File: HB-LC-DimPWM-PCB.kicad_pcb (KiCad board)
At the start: 2 copper layers, 73 parts, among them J1 SWD, J3 Conn_01x04_Male, Q1 S9013, Q10 BSS84, Q11 2N7002, Q12 BSS84, Q13 2N7002, Q14 VS5810AS, Q15 VS5810AS, Q16 VS5810AS, Q2 BSS84, Q3 2N7002, Q4 VS5810AS, Q5 S9013, Q6 S9013, Q7 S9013, Q8 BSS84, Q9 2N7002, U1 STM32F103C8Tx, U2 AMS1117-3.3, Y1 8MHz

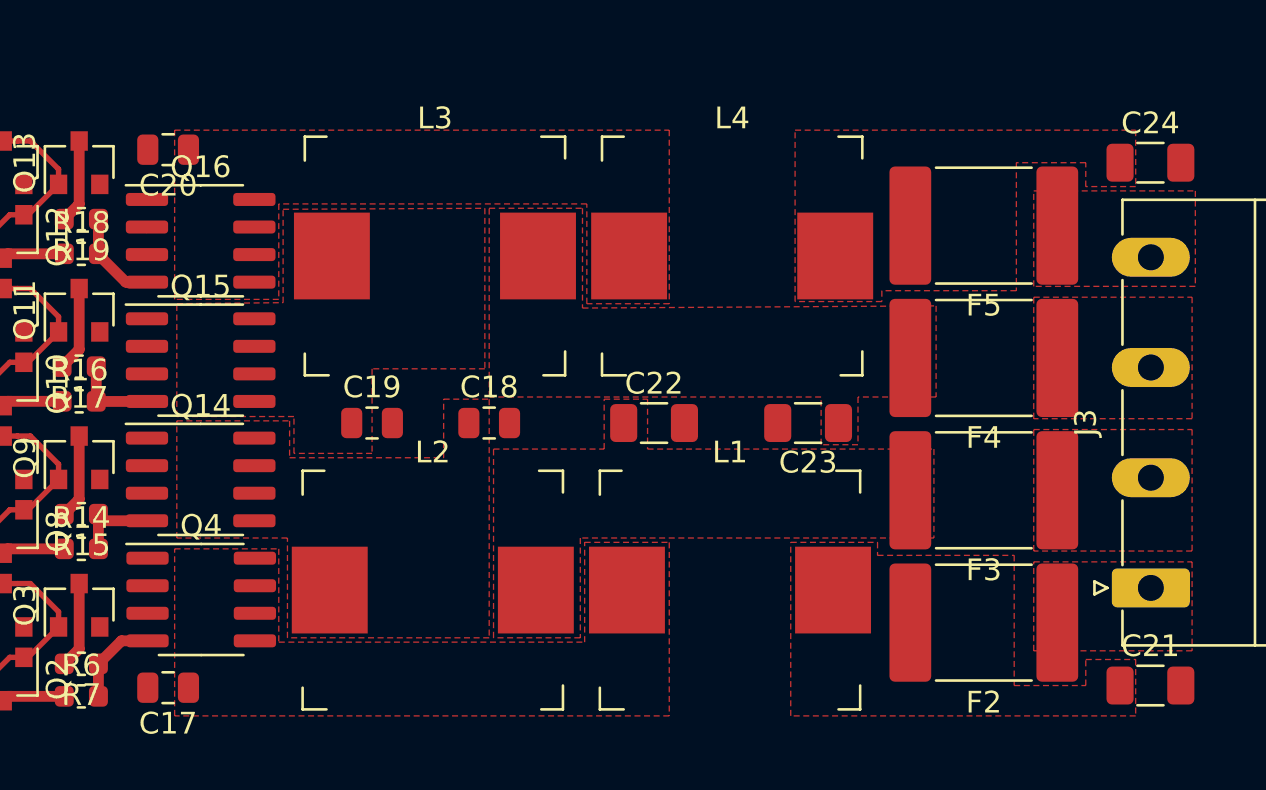
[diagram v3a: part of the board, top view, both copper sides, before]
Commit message: Add more space for GND vias below dimmer FETs
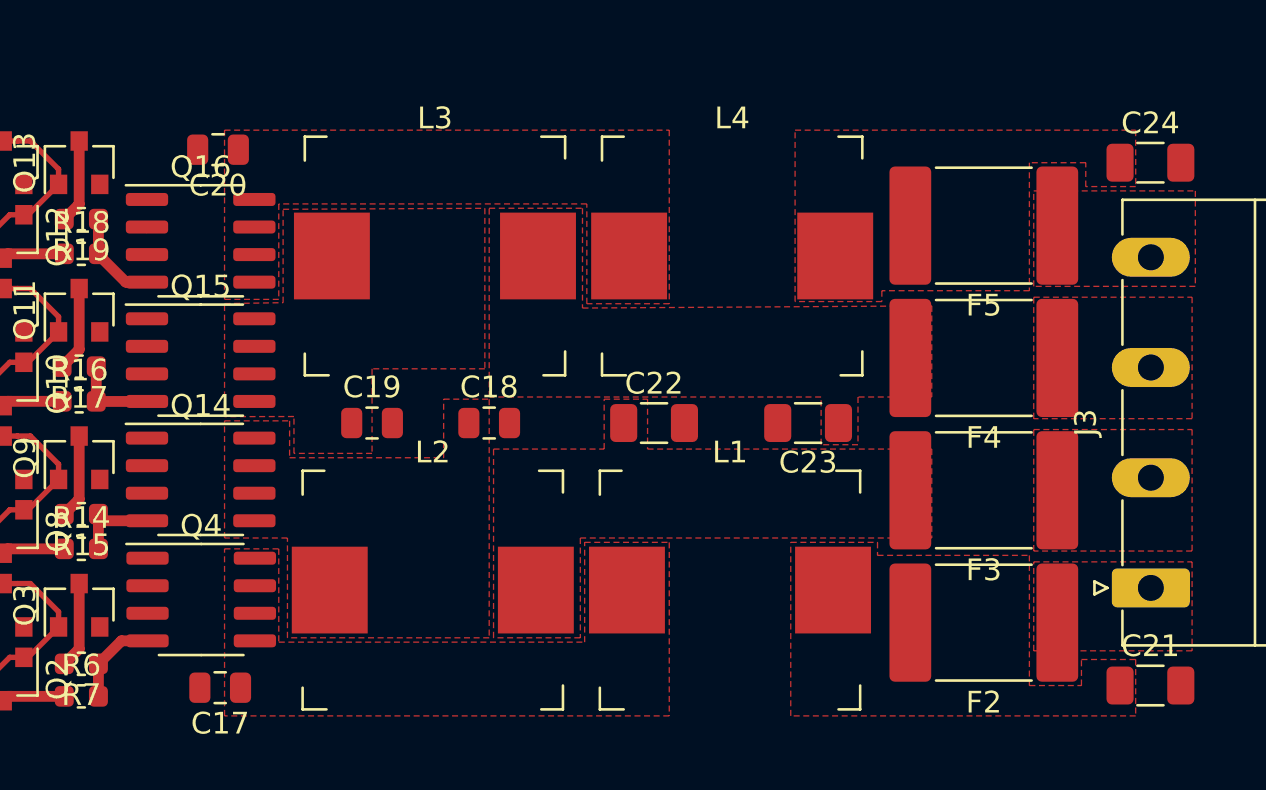
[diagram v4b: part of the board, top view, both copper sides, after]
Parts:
- moved C17 2.40 mm to (122.3, 92.6)
- moved C20 2.30 mm to (122.2, 67.8)
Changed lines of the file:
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@@
   )
   (module Capacitor_SMD:C_0805_2012Metric (layer F.Cu)
-    (at 119.9 67.8 180)
+    (at 122.2 67.8 180)
     (descr "Capacitor SMD 0805 (2012 Metric), square (rectangular) end terminal, IPC_7351 nominal, (Body size source: https://docs.google.com/spreadsheets/d/1BsfQQcO9C6DZCsRaXUlFlo91Tg2WpOkGARC1WS5S8t0/edit?usp=sharing), generated with kicad-footprint-generator")
     (tags capacitor)
@@
   )
   (module Capacitor_SMD:C_0805_2012Metric (layer F.Cu)
-    (at 119.9 92.6 180)
+    (at 122.3 92.6 180)
     (descr "Capacitor SMD 0805 (2012 Metric), square (rectangular) end terminal, IPC_7351 nominal, (Body size source: https://docs.google.com/spreadsheets/d/1BsfQQcO9C6DZCsRaXUlFlo91Tg2WpOkGARC1WS5S8t0/edit?usp=sharing), generated with kicad-footprint-generator")
     (tags capacitor)
@@
       (pts
         (xy 134.5 77.9) (xy 129.3 77.9) (xy 129.3 81.8) (xy 125.7 81.8) (xy 125.7 80.1)
-        (xy 120.3 80.1) (xy 120.3 74.9) (xy 125.2 74.852106) (xy 125.2 70.547894) (xy 134.5 70.501404)
+        (xy 122.5 80.105506) (xy 122.5 74.894494) (xy 125.2 74.852106) (xy 125.2 70.547894) (xy 134.5 70.501404)
       )
     )
@@
       (pts
         (xy 143 74.9) (xy 139.2 74.9) (xy 139.2 70.3) (xy 125 70.3) (xy 125.000533 74.7)
-        (xy 120.199467 74.7) (xy 120.2 66.9) (xy 143 66.9)
+        (xy 122.499734 74.7) (xy 122.500267 66.9) (xy 143 66.9)
       )
     )
@@
       (pts
         (xy 125.5 82) (xy 132.6 82) (xy 132.6 79.3) (xy 134.7 79.3) (xy 134.7 90.3)
-        (xy 125.4 90.3) (xy 125.4 85.7) (xy 120.3 85.700354) (xy 120.3 80.299646) (xy 125.5 80.300354)
+        (xy 125.4 90.3) (xy 125.4 85.7) (xy 122.5 85.700354) (xy 122.5 80.299646) (xy 125.5 80.300354)
       )
     )
@@
     (polygon
       (pts
-        (xy 143 93.9) (xy 120.2 93.9) (xy 120.2 86.2) (xy 125 86.2) (xy 125 90.5)
+        (xy 143 93.9) (xy 122.5 93.9) (xy 122.5 86.2) (xy 125 86.2) (xy 125 90.5)
         (xy 139.1 90.5) (xy 139.1 85.9) (xy 143 85.9)
       )
@@
     (polygon
       (pts
-        (xy 155.2 85.7) (xy 138.9 85.7) (xy 138.9 90.3) (xy 134.9 90.3) (xy 134.9 81.6)
-        (xy 140 81.6) (xy 140 79.3) (xy 142 79.3) (xy 142 81.6) (xy 155.2 81.6)
+        (xy 155.1 85.7) (xy 138.9 85.7) (xy 138.9 90.3) (xy 134.9 90.3) (xy 134.9 81.6)
+        (xy 140 81.6) (xy 140 79.3) (xy 142 79.3) (xy 142 81.6) (xy 155.1 81.6)
       )
     )
@@
     (polygon
       (pts
-        (xy 139 75.1) (xy 155.3 75) (xy 155.3 79.2) (xy 151.7 79.2) (xy 151.7 81.4)
+        (xy 139 75.1) (xy 155.1 75) (xy 155.1 79.2) (xy 151.7 79.2) (xy 151.7 81.4)
         (xy 150 81.4) (xy 150 79.2) (xy 134.7 79.2) (xy 134.7 70.5) (xy 139 70.5)
       )
@@
     (polygon
       (pts
-        (xy 164.501736 69.5) (xy 162.198264 69.5) (xy 162.2 68.4) (xy 159 68.4) (xy 159 74.3)
+        (xy 164.501736 69.5) (xy 162.198264 69.5) (xy 162.2 68.4) (xy 159.6 68.4) (xy 159.6 74.3)
         (xy 152.8 74.3) (xy 152.8 74.8) (xy 148.8 74.8) (xy 148.8 66.9) (xy 164.5 66.9)
       )
@@
     (polygon
       (pts
-        (xy 152.6 86.5) (xy 158.9 86.5) (xy 158.9 92.5) (xy 162.2 92.5) (xy 162.2 91.3)
+        (xy 152.6 86.5) (xy 159.6 86.5) (xy 159.6 92.5) (xy 162 92.5) (xy 162 91.3)
         (xy 164.5 91.3) (xy 164.5 93.9) (xy 148.6 93.9) (xy 148.6 85.9) (xy 152.6 85.9)
       )

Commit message: Add full layout as PoC
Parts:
- added C13: 1uF, Capacitor_SMD:C_0402_1005Metric, F.Cu at (148.5, 66.2)
- added C13: 1uF, Capacitor_SMD:C_0402_1005Metric, F.Cu at (148.5, 93.8)
- added C13: 1uF, Capacitor_SMD:C_0402_1005Metric, F.Cu at (196.7, 114.5)
- added C14: 1uF, Capacitor_SMD:C_0402_1005Metric, F.Cu at (148.5, 73.0)
- added C14: 1uF, Capacitor_SMD:C_0402_1005Metric, F.Cu at (148.5, 100.6)
- added C14: 1uF, Capacitor_SMD:C_0402_1005Metric, F.Cu at (196.7, 107.7)
- added C15: 1uF, Capacitor_SMD:C_0402_1005Metric, F.Cu at (148.5, 79.8)
- added C15: 1uF, Capacitor_SMD:C_0402_1005Metric, F.Cu at (148.5, 107.4)
- added C15: 1uF, Capacitor_SMD:C_0402_1005Metric, F.Cu at (196.7, 100.9)
- added C16: 1uF, Capacitor_SMD:C_0402_1005Metric, F.Cu at (148.6, 86.7)
- added C16: 1uF, Capacitor_SMD:C_0402_1005Metric, F.Cu at (148.6, 114.2)
- added C16: 1uF, Capacitor_SMD:C_0402_1005Metric, F.Cu at (196.7, 94.0)
- added C17: 100p, Capacitor_SMD:C_0805_2012Metric, F.Cu at (136.2, 64.2)
- added C17: 100p, Capacitor_SMD:C_0805_2012Metric, F.Cu at (136.2, 91.8)
- added C17: 100p, Capacitor_SMD:C_0805_2012Metric, F.Cu at (209.0, 116.5)
- added C18: 100p, Capacitor_SMD:C_0805_2012Metric, F.Cu at (123.8, 76.4)
- added C18: 100p, Capacitor_SMD:C_0805_2012Metric, F.Cu at (123.8, 104.0)
- added C18: 100p, Capacitor_SMD:C_0805_2012Metric, F.Cu at (221.4, 104.3)
- added C19: 100p, Capacitor_SMD:C_0805_2012Metric, F.Cu at (129.2, 76.4)
- added C19: 100p, Capacitor_SMD:C_0805_2012Metric, F.Cu at (129.2, 104.0)
- added C19: 100p, Capacitor_SMD:C_0805_2012Metric, F.Cu at (216.0, 104.3)
- added C20: 100p, Capacitor_SMD:C_0805_2012Metric, F.Cu at (136.3, 89.0)
- added C20: 100p, Capacitor_SMD:C_0805_2012Metric, F.Cu at (136.3, 116.6)
- added C20: 100p, Capacitor_SMD:C_0805_2012Metric, F.Cu at (208.9, 91.7)
- added C21: 1uF, Capacitor_SMD:C_1206_3216Metric, F.Cu at (93.3, 64.3)
- added C21: 1uF, Capacitor_SMD:C_1206_3216Metric, F.Cu at (93.3, 91.9)
- added C21: 1uF, Capacitor_SMD:C_1206_3216Metric, F.Cu at (251.9, 116.4)
- added C22: 1uF, Capacitor_SMD:C_1206_3216Metric, F.Cu at (116.2, 76.4)
- added C22: 1uF, Capacitor_SMD:C_1206_3216Metric, F.Cu at (116.2, 104.0)
- added C22: 1uF, Capacitor_SMD:C_1206_3216Metric, F.Cu at (229.0, 104.3)
- added C23: 1uF, Capacitor_SMD:C_1206_3216Metric, F.Cu at (109.1, 76.4)
- added C23: 1uF, Capacitor_SMD:C_1206_3216Metric, F.Cu at (109.1, 104.0)
- added C23: 1uF, Capacitor_SMD:C_1206_3216Metric, F.Cu at (236.1, 104.3)
- added C24: 1uF, Capacitor_SMD:C_1206_3216Metric, F.Cu at (93.3, 88.4)
- added C24: 1uF, Capacitor_SMD:C_1206_3216Metric, F.Cu at (93.3, 116.0)
- added C24: 1uF, Capacitor_SMD:C_1206_3216Metric, F.Cu at (251.9, 92.3)
- added F2: 15V 5A, Fuse:Fuse_2920_7451Metric, F.Cu at (101.0, 67.2)
- added F2: 15V 5A, Fuse:Fuse_2920_7451Metric, F.Cu at (101.0, 94.8)
- added F2: 15V 5A, Fuse:Fuse_2920_7451Metric, F.Cu at (244.2, 113.5)
- added F3: 15V 5A, Fuse:Fuse_2920_7451Metric, F.Cu at (101.0, 73.3)
- added F3: 15V 5A, Fuse:Fuse_2920_7451Metric, F.Cu at (101.0, 100.9)
- added F3: 15V 5A, Fuse:Fuse_2920_7451Metric, F.Cu at (244.2, 107.4)
- added F4: 15V 5A, Fuse:Fuse_2920_7451Metric, F.Cu at (101.0, 79.4)
- added F4: 15V 5A, Fuse:Fuse_2920_7451Metric, F.Cu at (101.0, 107.0)
- added F4: 15V 5A, Fuse:Fuse_2920_7451Metric, F.Cu at (244.2, 101.3)
- added F5: 15V 5A, Fuse:Fuse_2920_7451Metric, F.Cu at (101.0, 85.5)
- added F5: 15V 5A, Fuse:Fuse_2920_7451Metric, F.Cu at (101.0, 113.1)
- added F5: 15V 5A, Fuse:Fuse_2920_7451Metric, F.Cu at (244.2, 95.2)
- added J3: Conn_01x04_Male, Connector_Phoenix_MC_HighVoltage:PhoenixContact_MC_1,5_4-G-5.08_1x04_P5.08mm_Horizontal, F.Cu at (93.3, 68.8)
- added J3: Conn_01x04_Male, Connector_Phoenix_MC_HighVoltage:PhoenixContact_MC_1,5_4-G-5.08_1x04_P5.08mm_Horizontal, F.Cu at (93.3, 96.4)
- added J3: Conn_01x04_Male, Connector_Phoenix_MC_HighVoltage:PhoenixContact_MC_1,5_4-G-5.08_1x04_P5.08mm_Horizontal, F.Cu at (251.9, 111.9)
- added L1: 3.3uH, Inductor_Sunlord:SMD-PIND-10.5x11.5x4_2.5x3.0, F.Cu at (112.7, 68.7)
- added L1: 3.3uH, Inductor_Sunlord:SMD-PIND-10.5x11.5x4_2.5x3.0, F.Cu at (112.7, 96.3)
- added L1: 3.3uH, Inductor_Sunlord:SMD-PIND-10.5x11.5x4_2.5x3.0, F.Cu at (232.5, 112.0)
- added L2: 3.3uH, Inductor_Sunlord:SMD-PIND-10.5x11.5x4_2.5x3.0, F.Cu at (126.4, 68.7)
- added L2: 3.3uH, Inductor_Sunlord:SMD-PIND-10.5x11.5x4_2.5x3.0, F.Cu at (126.4, 96.3)
- added L2: 3.3uH, Inductor_Sunlord:SMD-PIND-10.5x11.5x4_2.5x3.0, F.Cu at (218.8, 112.0)
- added L3: 3.3uH, Inductor_Sunlord:SMD-PIND-10.5x11.5x4_2.5x3.0, F.Cu at (126.3, 84.1)
- added L3: 3.3uH, Inductor_Sunlord:SMD-PIND-10.5x11.5x4_2.5x3.0, F.Cu at (126.3, 111.7)
- added L3: 3.3uH, Inductor_Sunlord:SMD-PIND-10.5x11.5x4_2.5x3.0, F.Cu at (218.9, 96.6)
- added L4: 3.3uH, Inductor_Sunlord:SMD-PIND-10.5x11.5x4_2.5x3.0, F.Cu at (112.6, 84.1)
- added L4: 3.3uH, Inductor_Sunlord:SMD-PIND-10.5x11.5x4_2.5x3.0, F.Cu at (112.6, 111.7)
- added L4: 3.3uH, Inductor_Sunlord:SMD-PIND-10.5x11.5x4_2.5x3.0, F.Cu at (232.6, 96.6)
- added Q1: S9013, Package_TO_SOT_SMD:SOT-23, F.Cu at (146.2, 68.0)
- added Q1: S9013, Package_TO_SOT_SMD:SOT-23, F.Cu at (146.2, 95.6)
- added Q1: S9013, Package_TO_SOT_SMD:SOT-23, F.Cu at (199.0, 112.7)
- added Q10: BSS84, Package_TO_SOT_SMD:SOT-23, F.Cu at (146.2, 78.2)
- added Q10: BSS84, Package_TO_SOT_SMD:SOT-23, F.Cu at (146.2, 105.8)
- added Q10: BSS84, Package_TO_SOT_SMD:SOT-23, F.Cu at (199.0, 102.5)
- added Q11: 2N7002, Package_TO_SOT_SMD:SOT-23, F.Cu at (142.7, 81.6)
- added Q11: 2N7002, Package_TO_SOT_SMD:SOT-23, F.Cu at (142.7, 109.2)
- added Q11: 2N7002, Package_TO_SOT_SMD:SOT-23, F.Cu at (202.5, 99.1)
- added Q12: BSS84, Package_TO_SOT_SMD:SOT-23, F.Cu at (146.2, 85.0)
- added Q12: BSS84, Package_TO_SOT_SMD:SOT-23, F.Cu at (146.2, 112.6)
- added Q12: BSS84, Package_TO_SOT_SMD:SOT-23, F.Cu at (199.0, 95.7)
- added Q13: 2N7002, Package_TO_SOT_SMD:SOT-23, F.Cu at (142.7, 88.4)
- added Q13: 2N7002, Package_TO_SOT_SMD:SOT-23, F.Cu at (142.7, 116.0)
- added Q13: 2N7002, Package_TO_SOT_SMD:SOT-23, F.Cu at (202.5, 92.3)
- added Q14: VS5810AS, Package_SO:SOIC-8_3.9x4.9mm_P1.27mm, F.Cu at (137.1, 73.8)
- added Q14: VS5810AS, Package_SO:SOIC-8_3.9x4.9mm_P1.27mm, F.Cu at (137.1, 101.4)
- added Q14: VS5810AS, Package_SO:SOIC-8_3.9x4.9mm_P1.27mm, F.Cu at (208.1, 106.9)
- added Q15: VS5810AS, Package_SO:SOIC-8_3.9x4.9mm_P1.27mm, F.Cu at (137.1, 79.3)
- added Q15: VS5810AS, Package_SO:SOIC-8_3.9x4.9mm_P1.27mm, F.Cu at (137.1, 106.9)
- added Q15: VS5810AS, Package_SO:SOIC-8_3.9x4.9mm_P1.27mm, F.Cu at (208.1, 101.4)
- added Q16: VS5810AS, Package_SO:SOIC-8_3.9x4.9mm_P1.27mm, F.Cu at (137.1, 84.8)
- added Q16: VS5810AS, Package_SO:SOIC-8_3.9x4.9mm_P1.27mm, F.Cu at (137.1, 112.4)
- added Q16: VS5810AS, Package_SO:SOIC-8_3.9x4.9mm_P1.27mm, F.Cu at (208.1, 95.9)
- added Q2: BSS84, Package_TO_SOT_SMD:SOT-23, F.Cu at (146.2, 64.6)
- added Q2: BSS84, Package_TO_SOT_SMD:SOT-23, F.Cu at (146.2, 92.2)
- added Q2: BSS84, Package_TO_SOT_SMD:SOT-23, F.Cu at (199.0, 116.1)
- added Q3: 2N7002, Package_TO_SOT_SMD:SOT-23, F.Cu at (142.7, 68.0)
- added Q3: 2N7002, Package_TO_SOT_SMD:SOT-23, F.Cu at (142.7, 95.6)
- added Q3: 2N7002, Package_TO_SOT_SMD:SOT-23, F.Cu at (202.5, 112.7)
- added Q4: VS5810AS, Package_SO:SOIC-8_3.9x4.9mm_P1.27mm, F.Cu at (137.1, 68.3)
- added Q4: VS5810AS, Package_SO:SOIC-8_3.9x4.9mm_P1.27mm, F.Cu at (137.1, 95.9)
- added Q4: VS5810AS, Package_SO:SOIC-8_3.9x4.9mm_P1.27mm, F.Cu at (208.1, 112.4)
- added Q5: S9013, Package_TO_SOT_SMD:SOT-23, F.Cu at (146.2, 74.8)
- added Q5: S9013, Package_TO_SOT_SMD:SOT-23, F.Cu at (146.2, 102.4)
- added Q5: S9013, Package_TO_SOT_SMD:SOT-23, F.Cu at (199.0, 105.9)
- added Q6: S9013, Package_TO_SOT_SMD:SOT-23, F.Cu at (146.2, 81.6)
- added Q6: S9013, Package_TO_SOT_SMD:SOT-23, F.Cu at (146.2, 109.2)
- added Q6: S9013, Package_TO_SOT_SMD:SOT-23, F.Cu at (199.0, 99.1)
- added Q7: S9013, Package_TO_SOT_SMD:SOT-23, F.Cu at (146.2, 88.4)
- added Q7: S9013, Package_TO_SOT_SMD:SOT-23, F.Cu at (146.2, 116.0)
- added Q7: S9013, Package_TO_SOT_SMD:SOT-23, F.Cu at (199.0, 92.3)
- added Q8: BSS84, Package_TO_SOT_SMD:SOT-23, F.Cu at (146.2, 71.4)
- added Q8: BSS84, Package_TO_SOT_SMD:SOT-23, F.Cu at (146.2, 99.0)
- added Q8: BSS84, Package_TO_SOT_SMD:SOT-23, F.Cu at (199.0, 109.3)
- added Q9: 2N7002, Package_TO_SOT_SMD:SOT-23, F.Cu at (142.7, 74.8)
- added Q9: 2N7002, Package_TO_SOT_SMD:SOT-23, F.Cu at (142.7, 102.4)
- added Q9: 2N7002, Package_TO_SOT_SMD:SOT-23, F.Cu at (202.5, 105.9)
- added R10: 10k, Resistor_SMD:R_0402_1005Metric, F.Cu at (148.6, 88.7)
- added R10: 10k, Resistor_SMD:R_0402_1005Metric, F.Cu at (148.6, 116.2)
- added R10: 10k, Resistor_SMD:R_0402_1005Metric, F.Cu at (196.7, 92.0)
- added R11: 1k, Resistor_SMD:R_0402_1005Metric, F.Cu at (148.5, 71.0)
- added R11: 1k, Resistor_SMD:R_0402_1005Metric, F.Cu at (148.5, 98.6)
- added R11: 1k, Resistor_SMD:R_0402_1005Metric, F.Cu at (196.7, 109.7)
- added R12: 1k, Resistor_SMD:R_0402_1005Metric, F.Cu at (148.5, 77.8)
- added R12: 1k, Resistor_SMD:R_0402_1005Metric, F.Cu at (148.5, 105.4)
- added R12: 1k, Resistor_SMD:R_0402_1005Metric, F.Cu at (196.7, 102.9)
- added R13: 1k, Resistor_SMD:R_0402_1005Metric, F.Cu at (148.6, 84.7)
- added R13: 1k, Resistor_SMD:R_0402_1005Metric, F.Cu at (148.6, 112.2)
- added R13: 1k, Resistor_SMD:R_0402_1005Metric, F.Cu at (196.7, 96.0)
- added R14: 22R, Resistor_SMD:R_0603_1608Metric, F.Cu at (142.6, 70.6)
- added R14: 22R, Resistor_SMD:R_0603_1608Metric, F.Cu at (142.6, 98.2)
- added R14: 22R, Resistor_SMD:R_0603_1608Metric, F.Cu at (202.6, 110.1)
- added R15: 22R, Resistor_SMD:R_0603_1608Metric, F.Cu at (142.6, 72.2)
- added R15: 22R, Resistor_SMD:R_0603_1608Metric, F.Cu at (142.6, 99.8)
- added R15: 22R, Resistor_SMD:R_0603_1608Metric, F.Cu at (202.6, 108.5)
- added R16: 22R, Resistor_SMD:R_0603_1608Metric, F.Cu at (142.7, 77.4)
- added R16: 22R, Resistor_SMD:R_0603_1608Metric, F.Cu at (142.7, 105.0)
- added R16: 22R, Resistor_SMD:R_0603_1608Metric, F.Cu at (202.5, 103.3)
- added R17: 22R, Resistor_SMD:R_0603_1608Metric, F.Cu at (142.7, 79.0)
- added R17: 22R, Resistor_SMD:R_0603_1608Metric, F.Cu at (142.7, 106.6)
- added R17: 22R, Resistor_SMD:R_0603_1608Metric, F.Cu at (202.5, 101.7)
- added R18: 22R, Resistor_SMD:R_0603_1608Metric, F.Cu at (142.6, 84.2)
- added R18: 22R, Resistor_SMD:R_0603_1608Metric, F.Cu at (142.6, 111.8)
- added R18: 22R, Resistor_SMD:R_0603_1608Metric, F.Cu at (202.6, 96.5)
- added R19: 22R, Resistor_SMD:R_0603_1608Metric, F.Cu at (142.6, 85.8)
- added R19: 22R, Resistor_SMD:R_0603_1608Metric, F.Cu at (142.6, 113.4)
- added R19: 22R, Resistor_SMD:R_0603_1608Metric, F.Cu at (202.6, 94.9)
- added R4: 10k, Resistor_SMD:R_0402_1005Metric, F.Cu at (148.5, 68.2)
- added R4: 10k, Resistor_SMD:R_0402_1005Metric, F.Cu at (148.5, 95.8)
- added R4: 10k, Resistor_SMD:R_0402_1005Metric, F.Cu at (196.7, 112.5)
- added R5: 1k, Resistor_SMD:R_0402_1005Metric, F.Cu at (148.5, 64.2)
- added R5: 1k, Resistor_SMD:R_0402_1005Metric, F.Cu at (148.5, 91.8)
- added R5: 1k, Resistor_SMD:R_0402_1005Metric, F.Cu at (196.7, 116.5)
- added R6: 22R, Resistor_SMD:R_0603_1608Metric, F.Cu at (142.6, 63.8)
- added R6: 22R, Resistor_SMD:R_0603_1608Metric, F.Cu at (142.6, 91.4)
- added R6: 22R, Resistor_SMD:R_0603_1608Metric, F.Cu at (202.6, 116.9)
- added R7: 22R, Resistor_SMD:R_0603_1608Metric, F.Cu at (142.6, 65.3)
- added R7: 22R, Resistor_SMD:R_0603_1608Metric, F.Cu at (142.6, 92.9)
- added R7: 22R, Resistor_SMD:R_0603_1608Metric, F.Cu at (202.6, 115.4)
- added R8: 10k, Resistor_SMD:R_0402_1005Metric, F.Cu at (148.5, 75.0)
- added R8: 10k, Resistor_SMD:R_0402_1005Metric, F.Cu at (148.5, 102.6)
- added R8: 10k, Resistor_SMD:R_0402_1005Metric, F.Cu at (196.7, 105.7)
- added R9: 10k, Resistor_SMD:R_0402_1005Metric, F.Cu at (148.5, 81.8)
- added R9: 10k, Resistor_SMD:R_0402_1005Metric, F.Cu at (148.5, 109.4)
- added R9: 10k, Resistor_SMD:R_0402_1005Metric, F.Cu at (196.7, 98.9)
- added U3: HomeMatic-sensor, HomeMatic-sensor:HomeMatic-sensor, F.Cu at (172.9, 90.1)
- moved C18 86.8 mm to (221.4, 76.7)
- moved J3 86.8 mm to (251.9, 84.3)
- moved L2 86.8 mm to (218.8, 84.4)
- moved L3 86.8 mm to (218.9, 69.0)
- moved C16 86.8 mm to (196.7, 66.5)
- moved C17 86.8 mm to (209.0, 88.9)
- moved C20 86.8 mm to (208.9, 64.1)
- moved Q1 86.8 mm to (199.0, 85.1)
- moved Q10 86.8 mm to (199.0, 74.9)
- moved Q11 86.8 mm to (202.5, 71.5)
- moved Q12 86.8 mm to (199.0, 68.1)
- moved Q13 86.8 mm to (202.5, 64.7)
- moved Q2 86.8 mm to (199.0, 88.5)
- moved Q3 86.8 mm to (202.5, 85.1)
- moved Q4 86.8 mm to (208.1, 84.8)
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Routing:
- net Net-(Q10-Pad1): track 10.0 -> 40.2 mm
- net Net-(Q5-Pad3): track 10.0 -> 40.2 mm
- net Net-(Q1-Pad3): track 10.0 -> 40.2 mm
- net Net-(Q12-Pad1): track 10.0 -> 40.1 mm
- net +12V: track 9.78 -> 39.1 mm
- net Net-(Q16-Pad4): track 4.50 -> 18.0 mm
- net Net-(Q4-Pad4): track 4.20 -> 16.8 mm
- net Net-(Q3-Pad3): track 3.98 -> 15.9 mm
- net Net-(Q14-Pad4): track 3.96 -> 15.9 mm
- net Net-(Q15-Pad4): track 3.94 -> 15.8 mm
- net Net-(Q11-Pad3): track 3.93 -> 15.7 mm
- net Net-(Q9-Pad3): track 3.88 -> 15.5 mm
- net Net-(Q13-Pad3): track 3.88 -> 15.5 mm
- net Net-(Q10-Pad3): track 2.94 -> 11.7 mm
- net Net-(Q8-Pad3): track 2.90 -> 11.6 mm
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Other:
- board outline added: 168.2 x 57 mm
